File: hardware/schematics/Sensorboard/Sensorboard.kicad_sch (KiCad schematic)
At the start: 85 parts, among them J1 Grauwasser, J2 Switch/Solder Jumper, J3 BME680 #0 Innen, J4 RS485, J5 BME280 #1 Außen, J6 HX711 GasWaage, J7 LT452 Malibu, J8 Frischwasser, J9 USB Power, Q1 IRLML2244, Q2 IRLML2244, Q3 IRLML2244, Q4 AO3401A, Q5 2N7002, Q6 IRLML2244, Q7 IRLML2244, U1 ESP32-S3-DevKitC, U2 TSR2-2450, U3 LDL1117S33R, U4 SP3485CP, U5 PCF8523T, U6 BNO055, U7 INA226, Y1 32.768, Y2 32.768

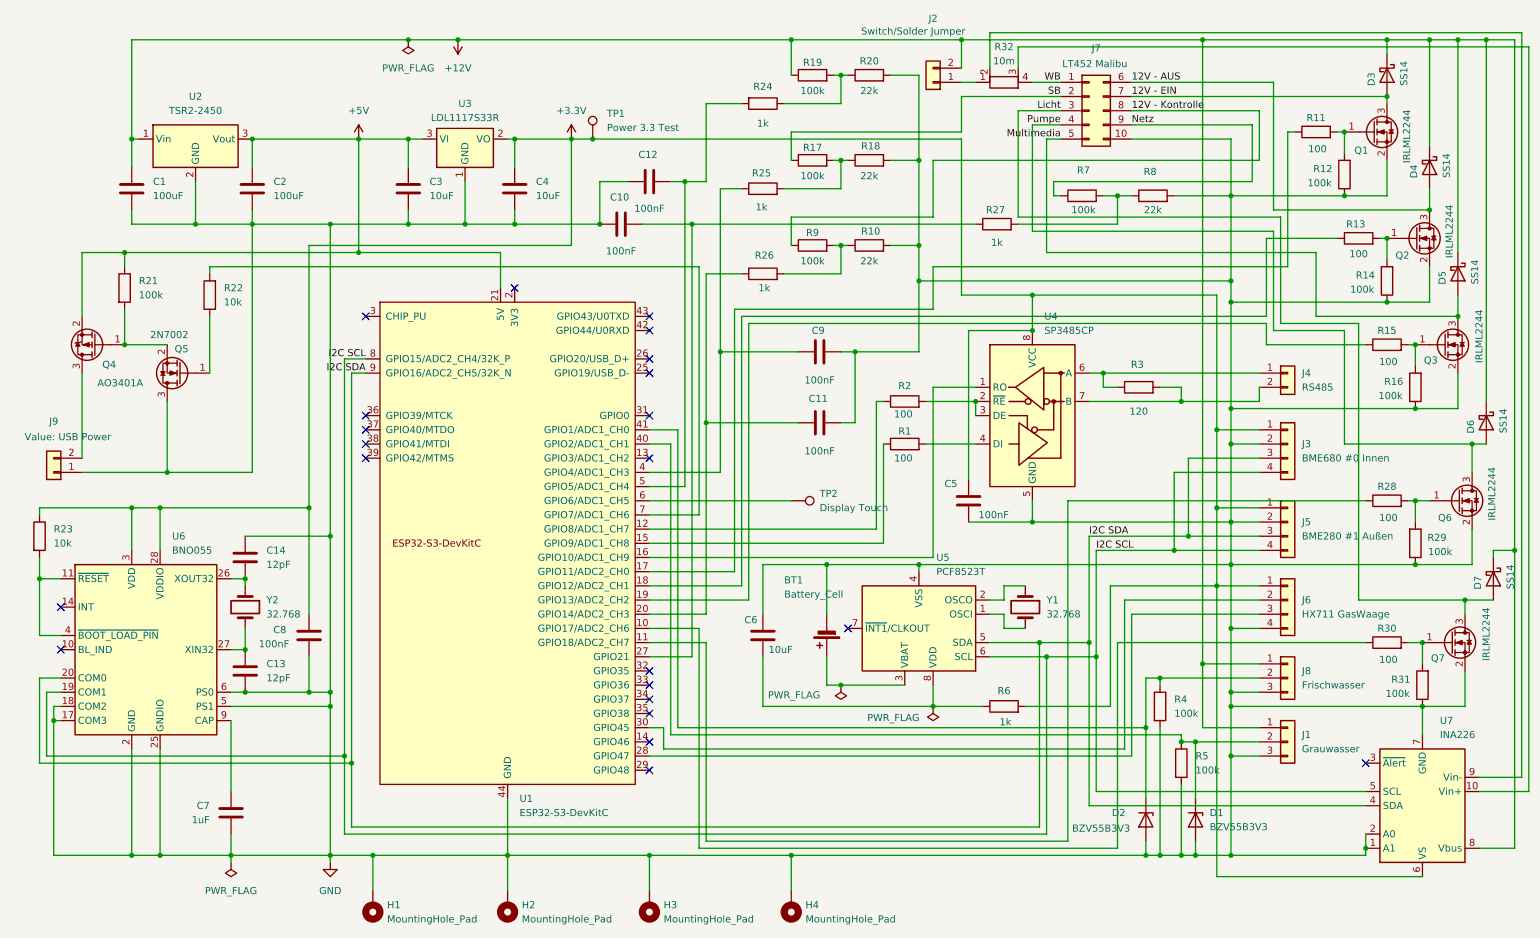
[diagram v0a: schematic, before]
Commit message: feat(sensorboard): RS485-Transceiver aus Schaltplan entfernt (ESP-NOW-Migration)
SP3485CP samt zugehöriger Beschaltung (Connector, R, C) aus
Sensorboard.kicad_sch entfernt, da die Display-Kommunikation auf
ESP-NOW umgestellt wird und der RS485-Transceiver nicht mehr
benötigt wird.
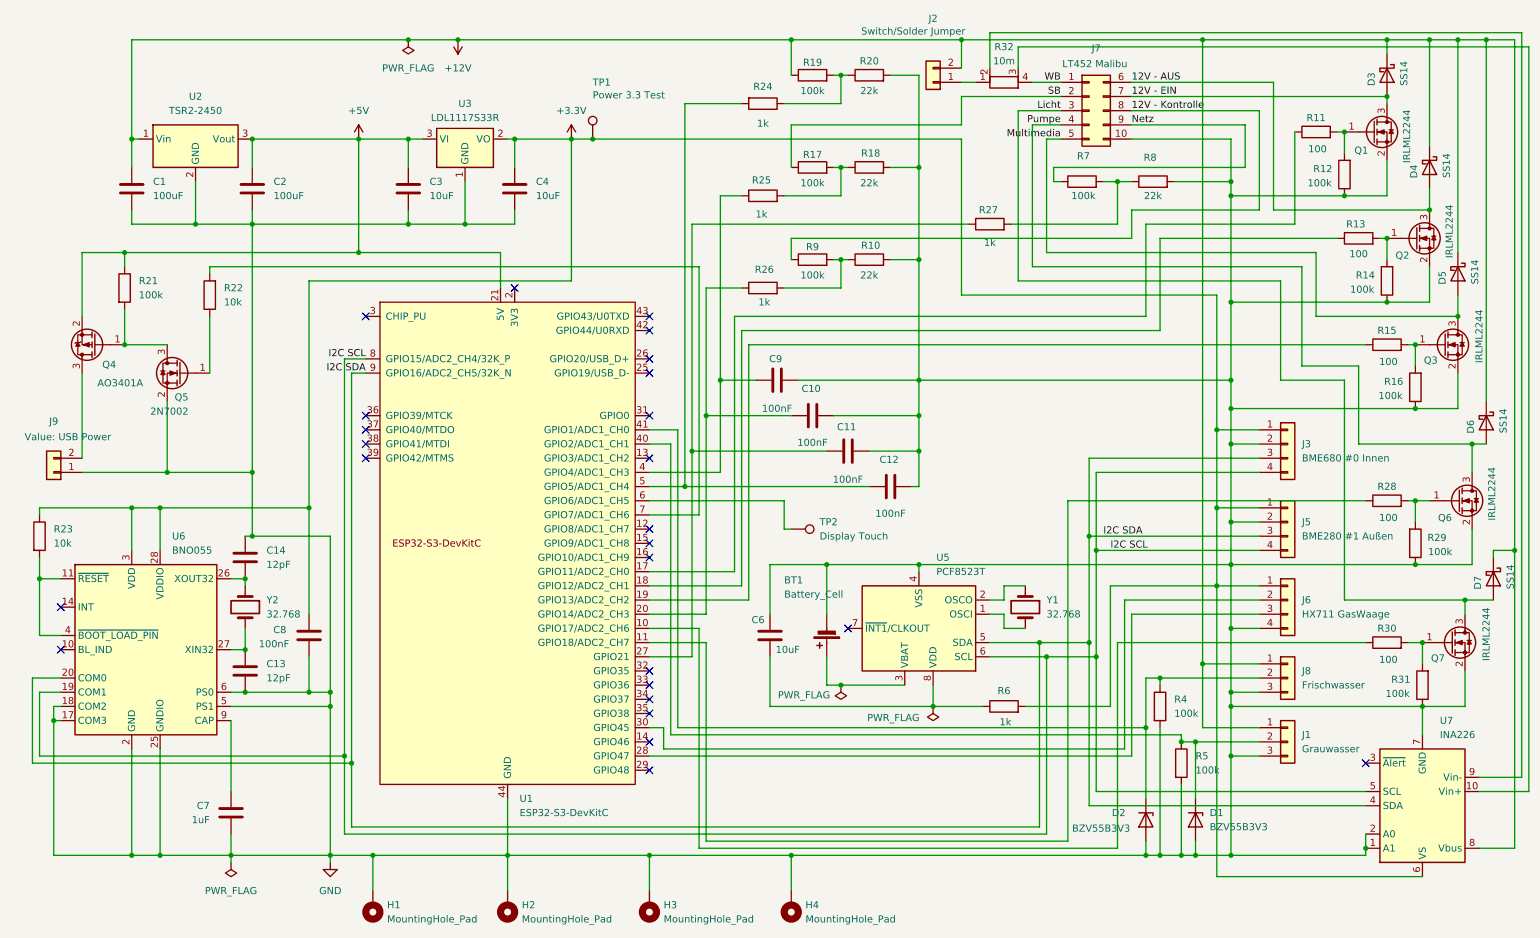
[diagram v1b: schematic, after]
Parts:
- removed C5: 100nF, Capacitor_SMD:C_0402_1005Metric, symbol Device:C
- removed J4: RS485, Connector_JST:JST_XH_B2B-XH-A_1x02_P2.50mm_Vertical, symbol Connector_Generic:Conn_01x02
- removed R1, R2: 100, Resistor_SMD:R_0402_1005Metric, symbol Device:R
- removed R3: 120, Resistor_SMD:R_0402_1005Metric, symbol Device:R
- removed U4: SP3485CP, Package_SO:SOIC-8_3.9x4.9mm_P1.27mm, symbol Interface_UART:SP3485CP
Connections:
- net GND: now also C10.1, C12.1, Q5.2 (S); no longer C10.2, C12.2, Q5.3 (D)
- net at R24.2, U1.5 (GPIO5/ADC1_CH4): now also C12.2; no longer C12.1
- net at Q4.1 (G), R21.2: now also Q5.3 (D); no longer Q5.2 (S)
- net at R27.1, U1.27 (GPIO21): now also C11.2; no longer C10.1
- net at R26.1, U1.20 (GPIO14/ADC2_CH3): now also C10.2; no longer C11.2
- no-connect marks 22 -> 25
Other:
- moved on the sheet: C10, C11, C12, C6, C9, Q5, R10, R17, R18, R25, R26, R27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
